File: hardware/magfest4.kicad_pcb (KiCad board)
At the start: 2 copper layers, 96.5 x 69.8 mm, 37 parts, among them J1 AVR-ISP-6, J2 AVR-ISP-6, J3 USB_B_Micro, P1 CONN_1, P6 CONN_1, P7 CONN_1, Q3 AP1117, U1 ATTINY25-45-85/DIP-SO, U2 ATTINY24-44-84/DIP-SO, X1 QUARTZCMS4

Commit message: Added LSCS parts
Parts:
- J3: footprint Connector_USB:USB_Micro-B_Amphenol_10118193-0001LF_Horizontal -> magfest4:AMPHENOL_10118192-0001LF
- U1: footprint Package_SO:SOIC-8_3.9x4.9mm_P1.27mm -> Package_SO:SOIC-8_5.23x5.23mm_P1.27mm
- X1: footprint Crystal:Crystal_SMD_1210-4Pin_1.2x1.0mm -> Crystal:Crystal_SMD_5032-2Pin_5.0x3.2mm
- moved J3 2.29 mm to (189.1, 138.8)
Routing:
- net GND: track 339.3 -> 333.0 mm
- net VCC: track 449.7 -> 450.4 mm
- net Net-(J3-D+): track 5.12 -> 5.78 mm
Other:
- board text added: "HOTDOG"
- board text added: "MAGF25-TY!"
- board text removed: "COPPER FRONT"
- board text removed: "MAGF11-XXXX"
- board text removed: "PCB EDGES"
- board text removed: "SILK SCREEN BACK (PLAIN SIDE)"
- board text removed: "SILK SCREEN FRONT"
- board text removed: "SOLDER MASK LAYER"
- board text removed: "UNUSED"
- board text removed: "[[Longer Names]]"

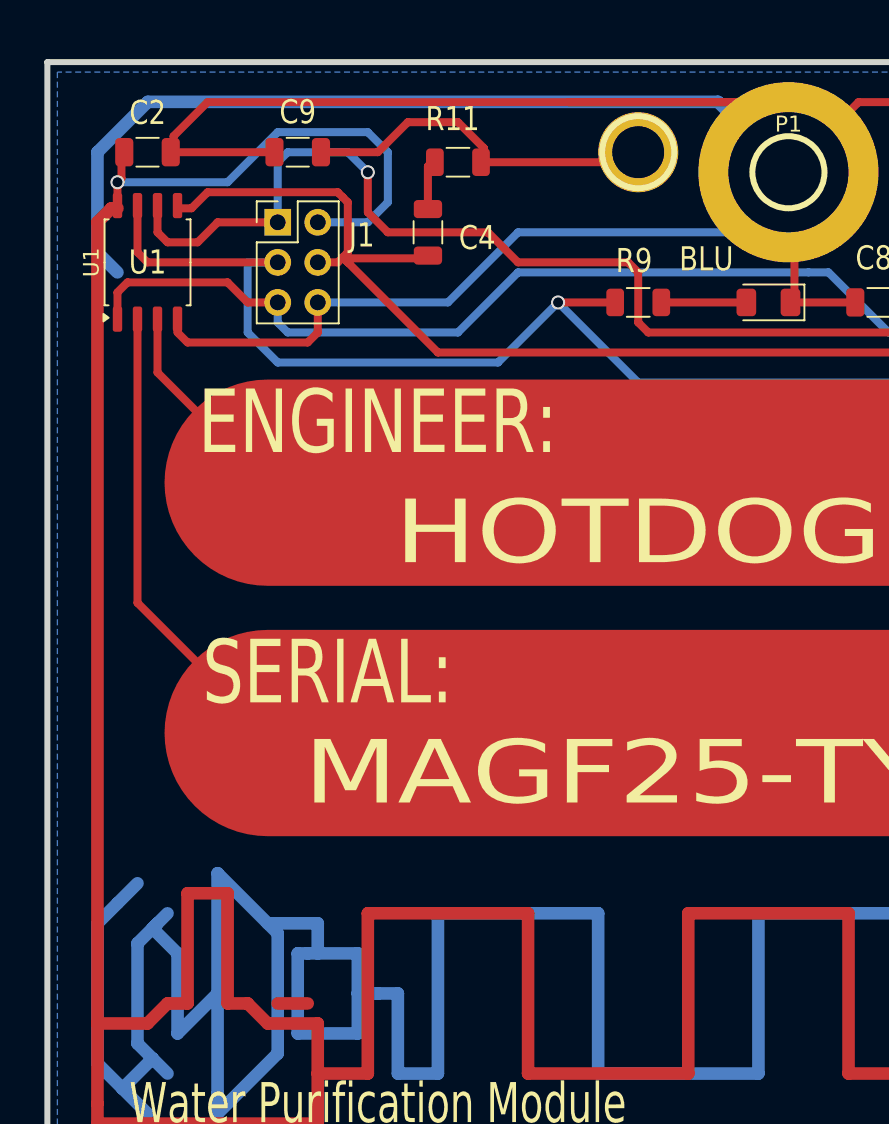
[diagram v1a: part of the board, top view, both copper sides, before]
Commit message: Fix parts for JLCPCB
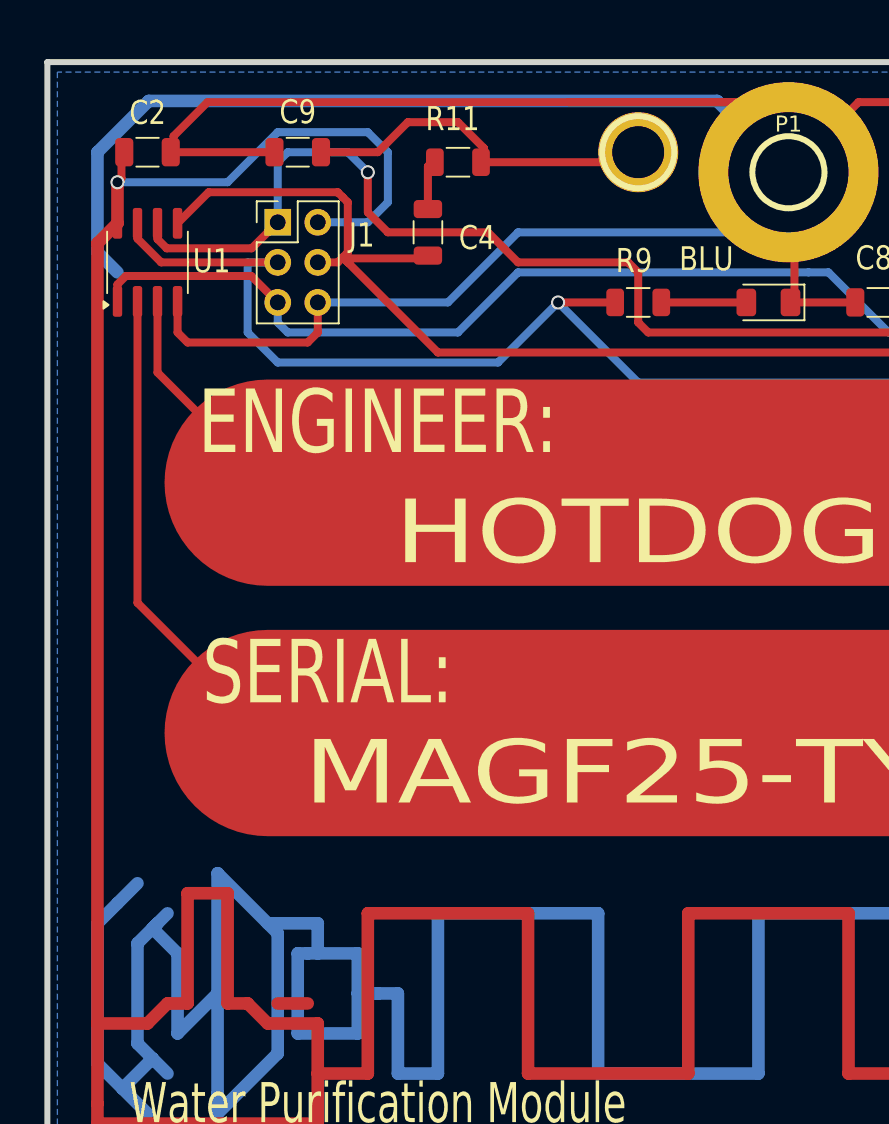
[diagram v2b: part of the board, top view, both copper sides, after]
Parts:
- U1: footprint Package_SO:SOIC-8_5.23x5.23mm_P1.27mm -> Package_SO:SOIC-8_3.9x4.9mm_P1.27mm
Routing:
- net /SCK: track 119.1 -> 117.7 mm
- net GND: track 333.0 -> 334.0 mm
- net /Touch2: track 87.9 -> 88.8 mm
- net /Touch1: track 80.6 -> 81.6 mm
